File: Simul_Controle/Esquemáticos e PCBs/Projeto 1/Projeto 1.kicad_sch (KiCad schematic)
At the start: 11 parts, among them J1 Conn_01x03_Pin, J2 Conn_01x02, J3 Conn_01x02, U2 LF355

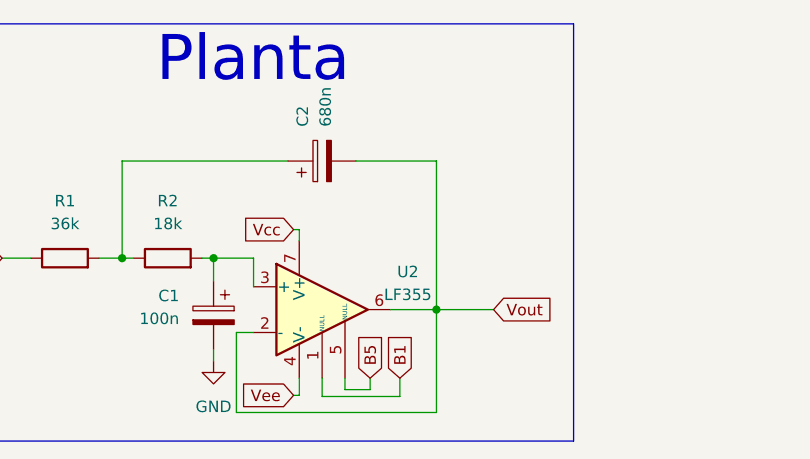
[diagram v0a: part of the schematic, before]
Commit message: Fixed typo on LF356 (previously 336) and added simulation for LF351, which was the closest available IC
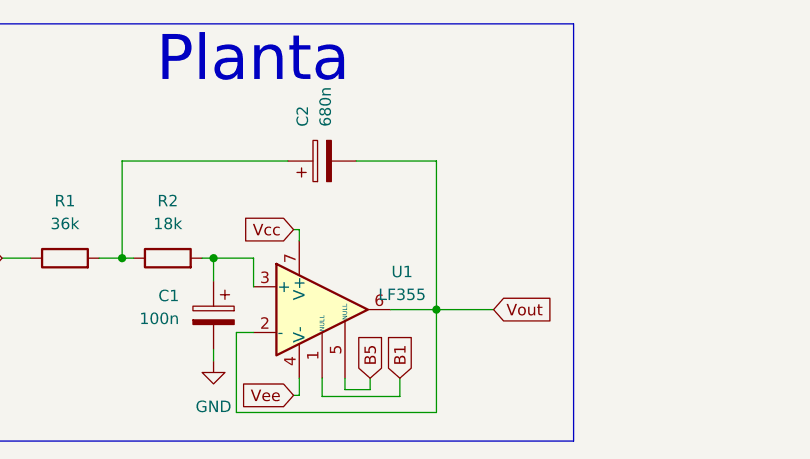
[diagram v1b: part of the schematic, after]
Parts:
- removed U2: LF355, Package_DIP:DIP-8_W7.62mm, symbol Amplifier_Operational:LF355
- added U1: LF355, Package_DIP:DIP-8_W7.62mm_LongPads, symbol Amplifier_Operational:LF355
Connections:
- net B1: now also U1.1 (NULL)
- net B5: now also U1.5 (NULL)
- net Vcc: now also U1.7 (V+)
- net Vee: now also U1.4 (V-)
- net Vout: now also U1.2 (-), U1.6
- net at C1.1, R2.2: now also U1.3 (+)
